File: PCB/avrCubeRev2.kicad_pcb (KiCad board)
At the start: 2 copper layers, 61.6 x 63.5 mm, 24 parts, among them J2 Conn_01x06_Male, SW1 SW_Push, U1 ATtiny24-20PU, U2 MMA8653FCR1

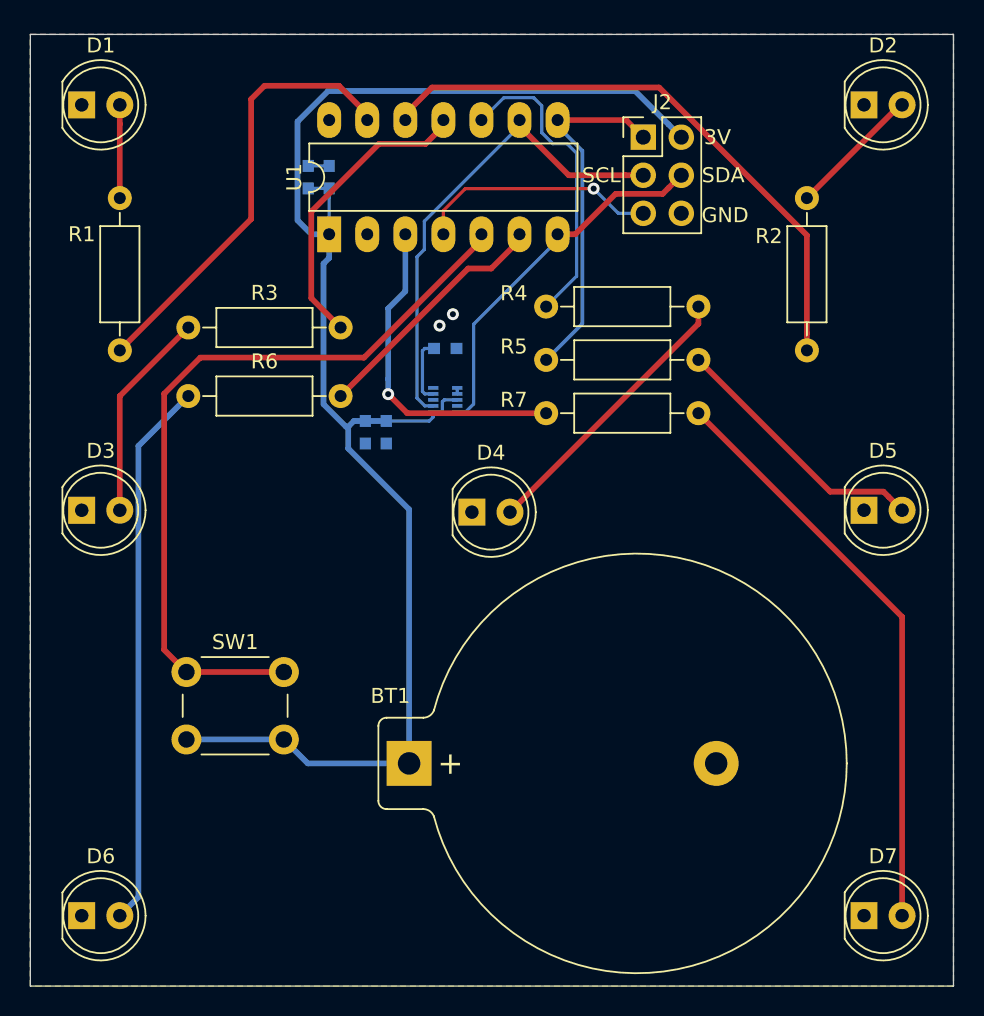
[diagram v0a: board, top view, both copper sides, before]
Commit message: Exported Gerber, Added Comments, Added Doxygen
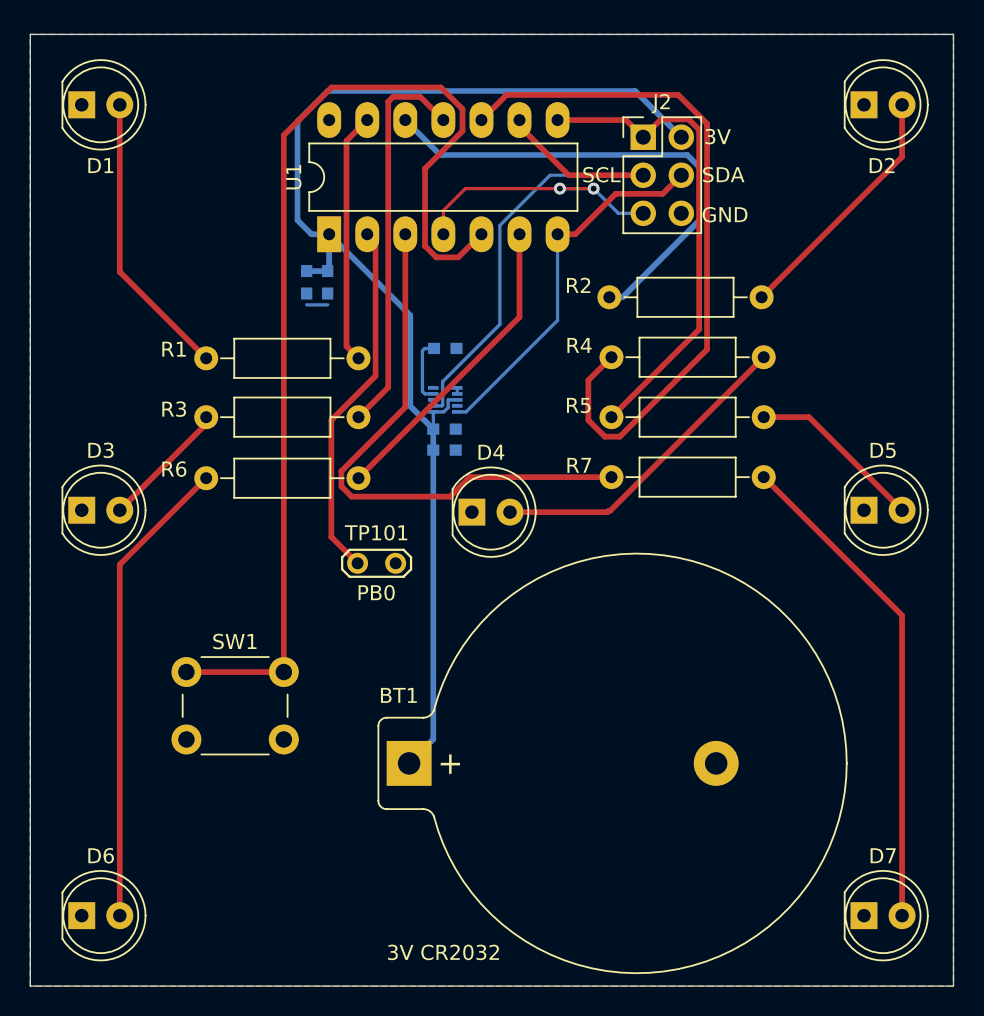
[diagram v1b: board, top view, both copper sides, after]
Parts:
- added TP101: TestPoint, TestPoint:TestPoint_2Pads_Pitch2.54mm_Drill0.8mm, F.Cu at (72.0, 96.2)
- moved R1 12.1 mm to (61.9, 82.6), turned to 0 degrees
- moved R2 7.28 mm to (99.0, 78.5), turned to 180 degrees
- moved C1 7.17 mm to (68.6, 77.5), turned to -90 degrees
- moved C2 7.13 mm to (70.0, 77.5), turned to -90 degrees
- moved R3 6.10 mm to (61.9, 86.5)
- moved R7 6.10 mm to (99.1, 90.5)
- moved R5 5.80 mm to (99.1, 86.5)
- moved R6 5.61 mm to (61.9, 90.6)
- moved R4 5.51 mm to (99.1, 82.5)
- moved C4 5.42 mm to (77.8, 88.7), turned to 0 degrees
- moved C3 3.89 mm to (77.8, 87.3), turned to 0 degrees
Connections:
- SW1 pad 2: +3V3 -> GND
- U1 pad 2: unconnected-(U1-Pad2) -> Net-(U1-Pad2)
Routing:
- net Net-(R4-Pad2): track 20.6 -> 47.2 mm
- net Net-(U1-Pad2): track 0.00 -> 24.1 mm
- net +3V3: track 103.7 -> 82.7 mm
- net /BUTTON: track 51.5 -> 71.0 mm
- net Net-(R7-Pad2): track 22.2 -> 37.4 mm, vias 1 -> 0
- net Net-(D1-Pad2): track 6.22 -> 19.3 mm
- net Net-(R1-Pad2): track 29.7 -> 16.8 mm
- net /MISO: track 23.9 -> 32.3 mm
- net Net-(D2-Pad2): track 8.93 -> 16.9 mm
- net Net-(R2-Pad2): track 39.7 -> 32.6 mm
- net Net-(R3-Pad2): track 20.1 -> 26.3 mm
- net Net-(D7-Pad2): track 39.2 -> 33.1 mm
- net Net-(D5-Pad2): track 17.7 -> 11.8 mm
- net Net-(D3-Pad2): track 14.1 -> 8.60 mm
- net Net-(D6-Pad2): track 36.6 -> 31.6 mm
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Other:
- board text added: "3V CR2032"
- board text added: "Developed by Fabian Franz V09.22"
- board text added: "PB0"
- board text removed: "Developed by Fabian Franz V08.22"
